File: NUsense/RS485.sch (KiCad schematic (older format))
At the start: 15 parts, among them J18? MOLEX22-03-5045, U21? MAX3443ECSA+

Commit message: Change hierarchy layout
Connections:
- net DXL_485+_1 renamed DXL_485+
- net DXL_485-_1 renamed DXL_485-
- net DXL_DIR_1 renamed DXL_DIR
- net DXL_RXD_1 renamed DXL_RXD
- net DXL_TXD_1 renamed DXL_TXD
- net VDD5o0V renamed +5V
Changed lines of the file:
@@
 LIBS:valves
 LIBS:ADM6713RAKS
+LIBS:Header_Connectors
 LIBS:MPU6000
 LIBS:NUbots
 LIBS:STM32F746ZGT6
-LIBS:Header_Connectors
 LIBS:NUsense-cache
 EELAYER 25 0
@@
 	1    0    0    -1
 $EndComp
-Text GLabel 3750 2550 1    60   Input ~ 0
-VDD5o0V
 $Comp
 L R R?
@@
 	1    0    0    -1
 $EndComp
-Text GLabel 6100 3500 2    60   Input ~ 0
-VDD5o0V
 $Comp
 L R R?
@@
 	0    -1   -1   0
 $EndComp
-Text GLabel 3550 3600 0    60   Input ~ 0
-DXL_DIR_1
-Text GLabel 3550 3500 0    60   Input ~ 0
-DXL_TXD_1
-Text GLabel 3550 3200 0    60   Input ~ 0
-DXL_RXD_1
-Text GLabel 7200 3200 2    60   Input ~ 0
-DXL_485+_1
-Text GLabel 7200 3300 2    60   Input ~ 0
-DXL_485-_1
-Text GLabel 3550 4850 0    60   Input ~ 0
-DXL_485+_1
-Text GLabel 3550 4950 0    60   Input ~ 0
-DXL_485-_1
 $Comp
 L GND #PWR?
@@
 	1    0    0    -1
 $EndComp
-Text GLabel 3850 4450 1    60   Input ~ 0
-DXL_PWR
 $Comp
 L C C?
@@
 	1    0    0    -1
 $EndComp
-Text GLabel 4950 9150 3    60   Input ~ 0
-DXL_PWR
 $Comp
 L R R?
@@
 	1    0    0    -1
 $EndComp
+$Comp
+L +5V #PWR?
+U 1 1 5A6FDCF8
+P 3750 2550
+F 0 "#PWR?" H 3750 2400 50  0001 C CNN
+F 1 "+5V" H 3750 2690 50  0000 C CNN
+F 2 "" H 3750 2550 50  0001 C CNN
+F 3 "" H 3750 2550 50  0001 C CNN
+	1    3750 2550
+	1    0    0    -1
+$EndComp
+Text HLabel 3550 3200 0    60   BiDi ~ 0
+DXL_RXD
+Text HLabel 3550 3500 0    60   BiDi ~ 0
+DXL_TXD
+Text HLabel 3550 3600 0    60   Input ~ 0
+DXL_DIR
+Text Label 3850 4450 1    60   ~ 0
+DXL_PWR
+Text Label 4950 9150 3    60   ~ 0
+DXL_PWR
+$Comp
+L +5V #PWR?
+U 1 1 5A6FED8C
+P 6100 3500
+F 0 "#PWR?" H 6100 3350 50  0001 C CNN
+F 1 "+5V" H 6100 3640 50  0000 C CNN
+F 2 "" H 6100 3500 50  0001 C CNN
+F 3 "" H 6100 3500 50  0001 C CNN
+	1    6100 3500
+	0    1    1    0
+$EndComp
+Text Label 7200 3200 0    60   ~ 0
+DXL_485+
+Text Label 7200 3300 0    60   ~ 0
+DXL_485-
+Text Label 3550 4850 2    60   ~ 0
+DXL_485+
+Text Label 3550 4950 2    60   ~ 0
+DXL_485-
 $EndSCHEMATC

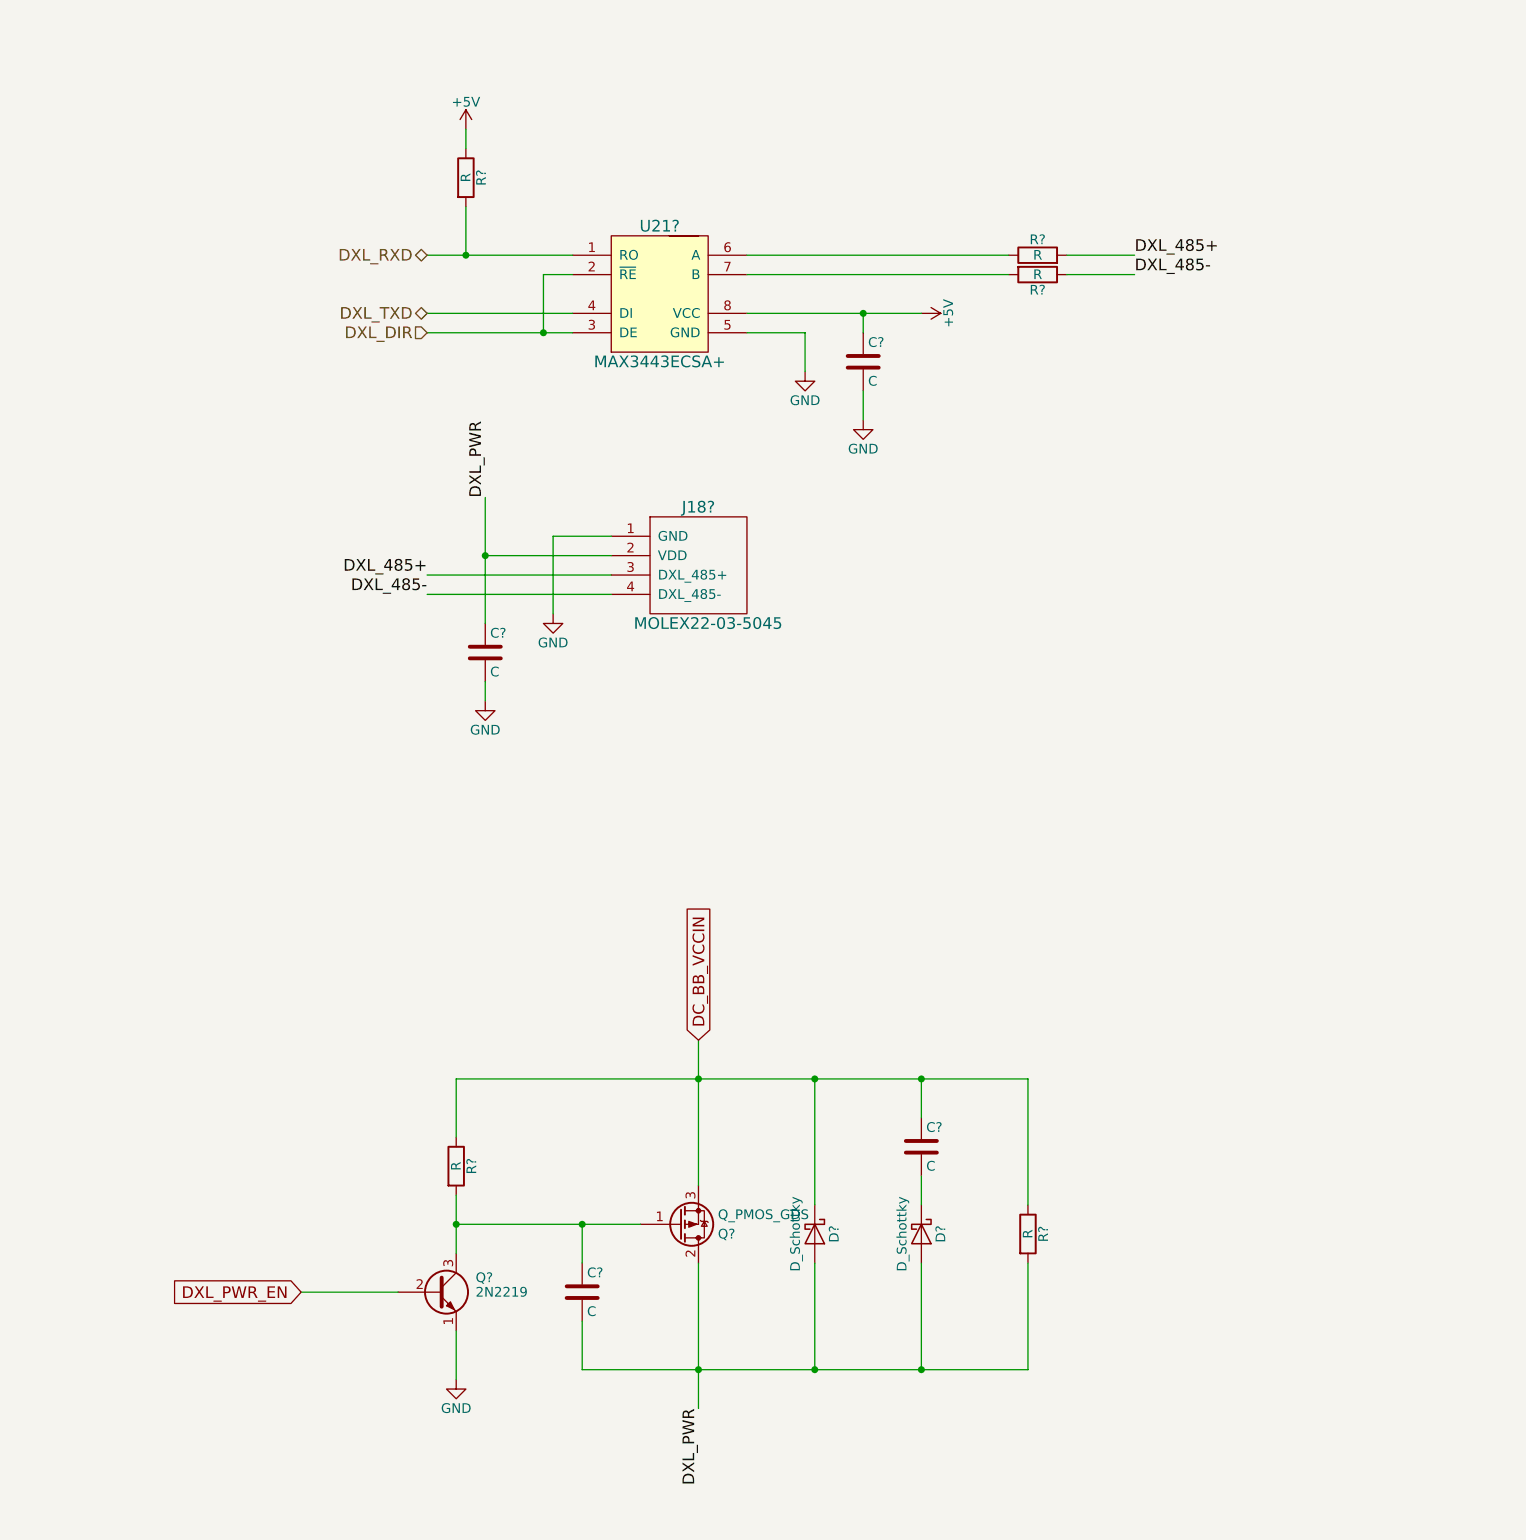
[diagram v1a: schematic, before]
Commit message: Update component values
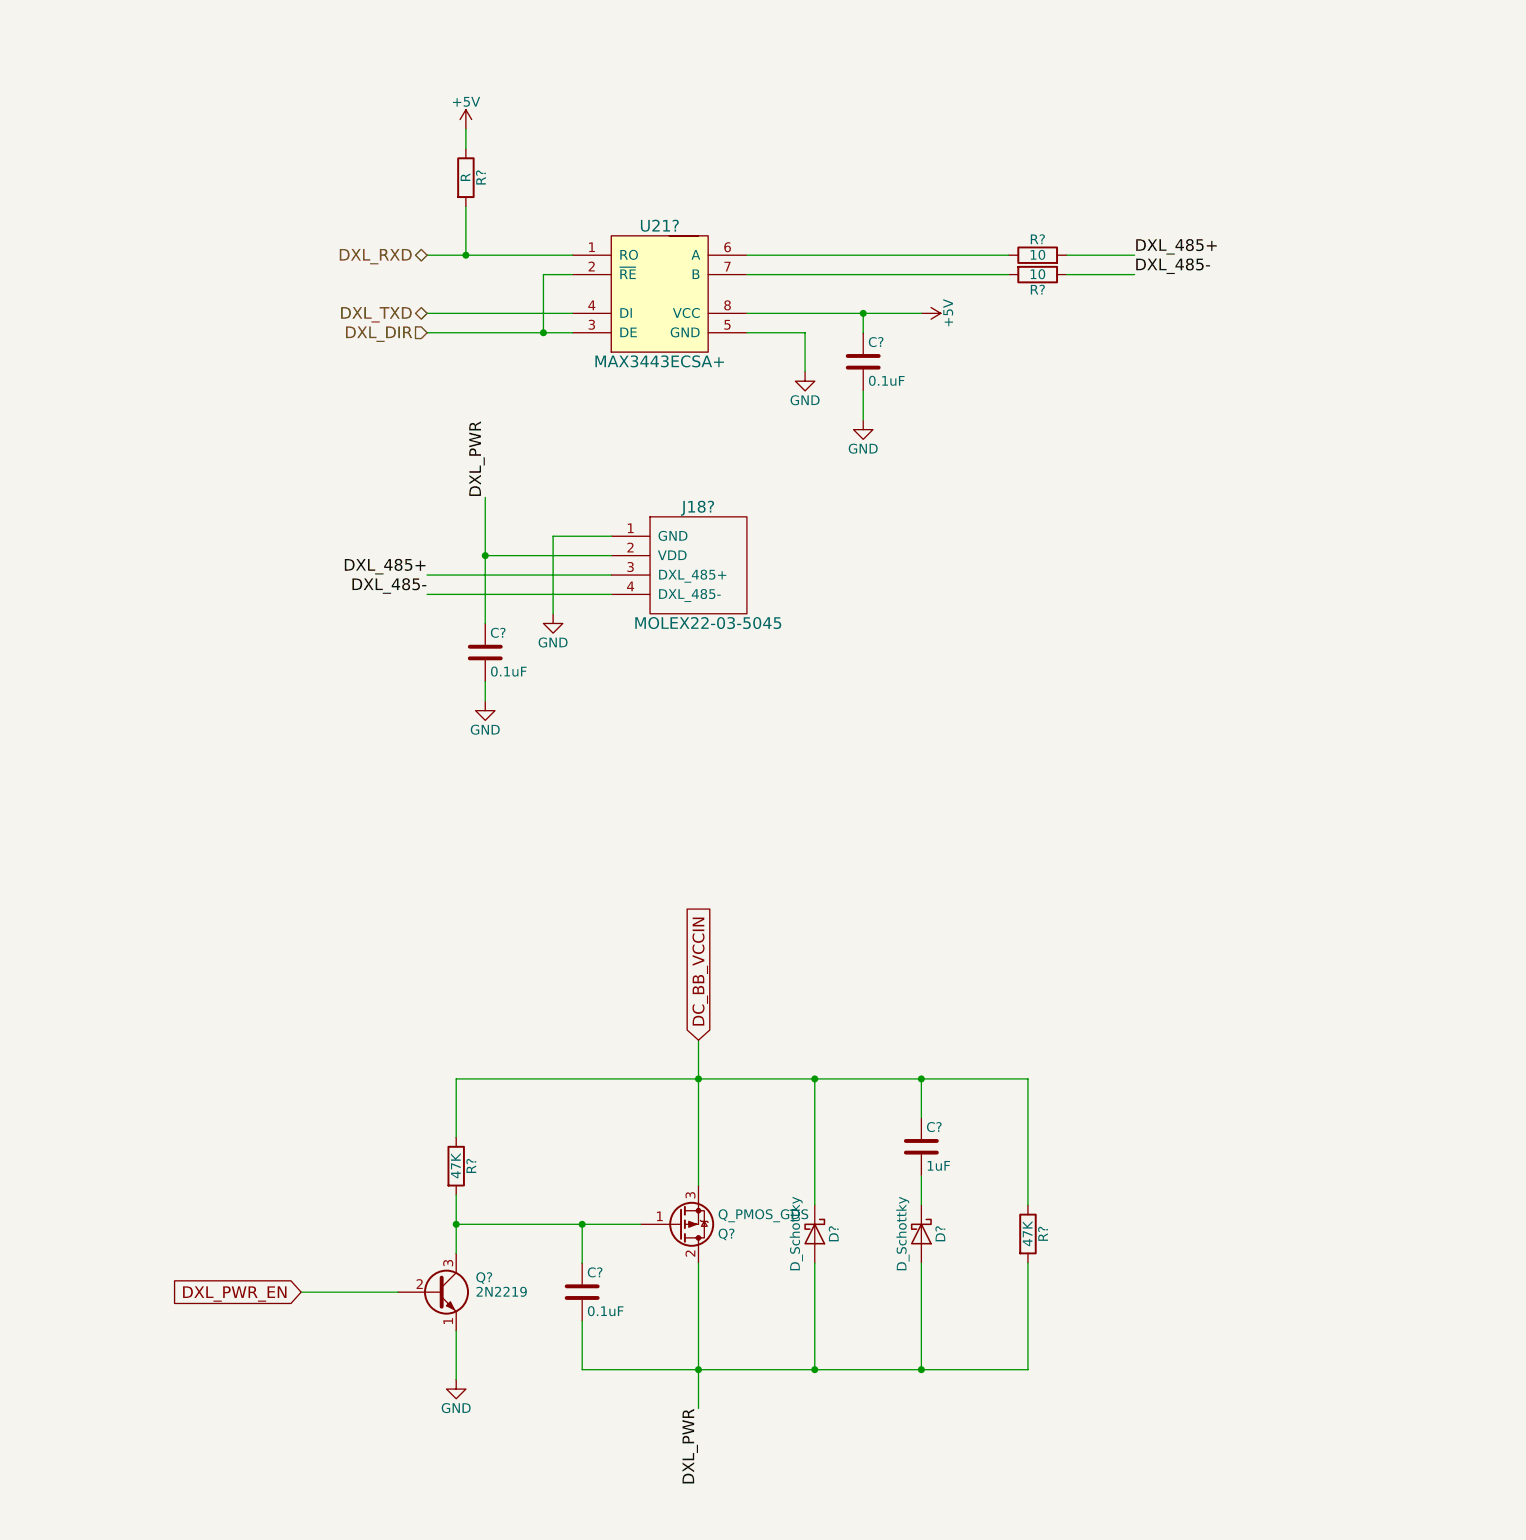
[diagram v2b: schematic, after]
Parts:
- C? (x3): value C -> 0.1uF
- C?: value C -> 1uF
- R? (x2): value R -> 10
- R? (x2): value R -> 47K
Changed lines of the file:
@@
 P 5800 3750
 F 0 "C?" H 5825 3850 50  0000 L CNN
-F 1 "C" H 5825 3650 50  0000 L CNN
+F 1 "0.1uF" H 5825 3650 50  0000 L CNN
 F 2 "" H 5838 3600 50  0001 C CNN
 F 3 "" H 5800 3750 50  0001 C CNN
@@
 P 6700 3300
 F 0 "R?" V 6780 3300 50  0000 C CNN
-F 1 "R" V 6700 3300 50  0000 C CNN
+F 1 "10" V 6700 3300 50  0000 C CNN
 F 2 "" V 6630 3300 50  0001 C CNN
 F 3 "" H 6700 3300 50  0001 C CNN
@@
 P 6700 3200
 F 0 "R?" V 6780 3200 50  0000 C CNN
-F 1 "R" V 6700 3200 50  0000 C CNN
+F 1 "10" V 6700 3200 50  0000 C CNN
 F 2 "" V 6630 3200 50  0001 C CNN
 F 3 "" H 6700 3200 50  0001 C CNN
@@
 P 3850 5250
 F 0 "C?" H 3875 5350 50  0000 L CNN
-F 1 "C" H 3875 5150 50  0000 L CNN
+F 1 "0.1uF" H 3875 5150 50  0000 L CNN
 F 2 "" H 3888 5100 50  0001 C CNN
 F 3 "" H 3850 5250 50  0001 C CNN
@@
 P 3700 7900
 F 0 "R?" V 3780 7900 50  0000 C CNN
-F 1 "R" V 3700 7900 50  0000 C CNN
+F 1 "47K" V 3700 7900 50  0000 C CNN
 F 2 "" V 3630 7900 50  0001 C CNN
 F 3 "" H 3700 7900 50  0001 C CNN
@@
 P 4350 8550
 F 0 "C?" H 4375 8650 50  0000 L CNN
-F 1 "C" H 4375 8450 50  0000 L CNN
+F 1 "0.1uF" H 4375 8450 50  0000 L CNN
 F 2 "" H 4388 8400 50  0001 C CNN
 F 3 "" H 4350 8550 50  0001 C CNN
@@
 P 6650 8250
 F 0 "R?" V 6730 8250 50  0000 C CNN
-F 1 "R" V 6650 8250 50  0000 C CNN
+F 1 "47K" V 6650 8250 50  0000 C CNN
 F 2 "" V 6580 8250 50  0001 C CNN
 F 3 "" H 6650 8250 50  0001 C CNN
@@
 P 6100 7800
 F 0 "C?" H 6125 7900 50  0000 L CNN
-F 1 "C" H 6125 7700 50  0000 L CNN
+F 1 "1uF" H 6125 7700 50  0000 L CNN
 F 2 "" H 6138 7650 50  0001 C CNN
 F 3 "" H 6100 7800 50  0001 C CNN

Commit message: Correct Broken Files
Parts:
- removed C?: 0.1uF, symbol C
- removed C?: 1uF, symbol C
- removed D? (x2): D_Schottky, symbol D_Schottky
- removed Q?: Q_PMOS_GDS, symbol Q_PMOS_GDS
- removed Q?: 2N2219, TO_SOT_Packages_THT:TO-39-3, symbol 2N2219
- removed R? (x2): 47K, symbol R
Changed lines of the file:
@@
-	1    0    0    -1
-$EndComp
-Text GLabel 2900 8550 0    60   Input ~ 0
-DXL_PWR_EN
-$Comp
-L R R?
-U 1 1 5A69947A
-P 3700 7900
-F 0 "R?" V 3780 7900 50  0000 C CNN
-F 1 "47K" V 3700 7900 50  0000 C CNN
-F 2 "" V 3630 7900 50  0001 C CNN
-F 3 "" H 3700 7900 50  0001 C CNN
-	1    3700 7900
-	1    0    0    -1
-$EndComp
-$Comp
-L C C?
-U 1 1 5A69952D
-P 4350 8550
-F 0 "C?" H 4375 8650 50  0000 L CNN
-F 1 "0.1uF" H 4375 8450 50  0000 L CNN
-F 2 "" H 4388 8400 50  0001 C CNN
-F 3 "" H 4350 8550 50  0001 C CNN
-	1    4350 8550
-	1    0    0    -1
-$EndComp
-$Comp
-L R R?
-U 1 1 5A699733
-P 6650 8250
-F 0 "R?" V 6730 8250 50  0000 C CNN
-F 1 "47K" V 6650 8250 50  0000 C CNN
-F 2 "" V 6580 8250 50  0001 C CNN
-F 3 "" H 6650 8250 50  0001 C CNN
-	1    6650 8250
-	1    0    0    -1
-$EndComp
-Text GLabel 4950 7250 1    60   Input ~ 0
-DC_BB_VCCIN
-$Comp
-L D_Schottky D?
-U 1 1 5A699A5F
-P 5550 8250
-F 0 "D?" H 5550 8350 50  0000 C CNN
-F 1 "D_Schottky" H 5550 8150 50  0000 C CNN
-F 2 "" H 5550 8250 50  0001 C CNN
-F 3 "" H 5550 8250 50  0001 C CNN
-	1    5550 8250
-	0    1    1    0
-$EndComp
-$Comp
-L D_Schottky D?
-U 1 1 5A699B12
-P 6100 8250
-F 0 "D?" H 6100 8350 50  0000 C CNN
-F 1 "D_Schottky" H 6100 8150 50  0000 C CNN
-F 2 "" H 6100 8250 50  0001 C CNN
-F 3 "" H 6100 8250 50  0001 C CNN
-	1    6100 8250
-	0    1    1    0
-$EndComp
-$Comp
-L C C?
-U 1 1 5A699B46
-P 6100 7800
-F 0 "C?" H 6125 7900 50  0000 L CNN
-F 1 "1uF" H 6125 7700 50  0000 L CNN
-F 2 "" H 6138 7650 50  0001 C CNN
-F 3 "" H 6100 7800 50  0001 C CNN
-	1    6100 7800
-	1    0    0    -1
-$EndComp
-$Comp
-L Q_PMOS_GDS Q?
-U 1 1 5A699B87
-P 4850 8200
-F 0 "Q?" H 5050 8250 50  0000 L CNN
-F 1 "Q_PMOS_GDS" H 5050 8150 50  0000 L CNN
-F 2 "" H 5050 8300 50  0001 C CNN
-F 3 "" H 4850 8200 50  0001 C CNN
-	1    4850 8200
-	1    0    0    1
-$EndComp
-$Comp
-L 2N2219 Q?
-U 1 1 5A69A90B
-P 3600 8550
-F 0 "Q?" H 3800 8625 50  0000 L CNN
-F 1 "2N2219" H 3800 8550 50  0000 L CNN
-F 2 "TO_SOT_Packages_THT:TO-39-3" H 3800 8475 50  0001 L CIN
-F 3 "" H 3600 8550 50  0001 L CNN
-	1    3600 8550
 	1    0    0    -1
 $EndComp
@@
 Wire Wire Line
 	4200 4650 4500 4650
-Wire Wire Line
-	4950 8400 4950 9150
-Wire Wire Line
-	4350 8950 6650 8950
-Wire Wire Line
-	4350 8950 4350 8700
-Wire Wire Line
-	6650 8950 6650 8400
-Connection ~ 4950 8950
-Wire Wire Line
-	3700 7750 3700 7450
-Wire Wire Line
-	3700 7450 6650 7450
-Wire Wire Line
-	6650 7450 6650 8100
-Wire Wire Line
-	4950 7250 4950 8000
-Connection ~ 4950 7450
-Wire Wire Line
-	4650 8200 3700 8200
-Wire Wire Line
-	4350 8400 4350 8200
-Connection ~ 4350 8200
-Wire Wire Line
-	5550 8100 5550 7450
-Connection ~ 5550 7450
-Wire Wire Line
-	6100 7650 6100 7450
-Connection ~ 6100 7450
-Wire Wire Line
-	6100 7950 6100 8100
-Wire Wire Line
-	6100 8400 6100 8950
-Connection ~ 6100 8950
-Wire Wire Line
-	5550 8400 5550 8950
-Connection ~ 5550 8950
-Wire Wire Line
-	3700 8050 3700 8350
-Connection ~ 3700 8200
-$Comp
-L GND #PWR?
-U 1 1 5A69AA92
-P 3700 9000
-F 0 "#PWR?" H 3700 8750 50  0001 C CNN
-F 1 "GND" H 3700 8850 50  0000 C CNN
-F 2 "" H 3700 9000 50  0001 C CNN
-F 3 "" H 3700 9000 50  0001 C CNN
-	1    3700 9000
-	1    0    0    -1
-$EndComp
-Wire Wire Line
-	3700 9000 3700 8750
-Wire Wire Line
-	3400 8550 2900 8550
 $Comp
 L MOLEX22-03-5045 J18?
@@
 Text HLabel 3550 3600 0    60   Input ~ 0
 DXL_DIR
-Text Label 3850 4450 1    60   ~ 0
-DXL_PWR
-Text Label 4950 9150 3    60   ~ 0
-DXL_PWR
 $Comp
 L +5V #PWR?
@@
 Text Label 3550 4950 2    60   ~ 0
 DXL_485-
+Text HLabel 3850 4450 0    60   Input ~ 0
+DXL_PWR
 $EndSCHEMATC

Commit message: ESD protection
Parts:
- added U?: AVRC5S_05D_050_050R, symbol AVRC5S_05D_050_050R
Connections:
- net DXL_RXD: now also U?.3 (B1); no longer R?.2, U21?.1 (RO)
- net DXL_TXD: now also U?.2 (A1); no longer U21?.4 (DI)
- net GND: now also U?.1 (GND)
- new net: R?.2, U21?.1 (RO), U?.6 (B2)
- new net: U21?.4 (DI), U?.5 (A2)
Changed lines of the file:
@@
 $EndComp
 Wire Wire Line
-	3550 3600 4300 3600
+	3550 3600 4150 3600
+Wire Wire Line
+	4150 3600 4300 3600
 Wire Wire Line
 	4300 3500 3550 3500
 Wire Wire Line
-	3550 3200 4300 3200
+	3550 3200 3750 3200
+Wire Wire Line
+	3750 3200 4300 3200
 Wire Wire Line
 	4300 3300 4150 3300
@@
 	5200 3300 6550 3300
 Wire Wire Line
-	5200 3500 6100 3500
+	5200 3500 5800 3500
+Wire Wire Line
+	5800 3500 6100 3500
 Wire Wire Line
 	5800 3600 5800 3500
@@
 	3850 5500 3850 5400
 Wire Wire Line
-	3850 4450 3850 5100
+	3850 4450 3850 4750
+Wire Wire Line
+	3850 4750 3850 5100
 Wire Wire Line
 	3850 4750 4500 4750
@@
 	1    0    0    -1
 $EndComp
-Text HLabel 3550 3200 0    60   BiDi ~ 0
+Text HLabel 1950 3300 0    60   BiDi ~ 0
 DXL_RXD
-Text HLabel 3550 3500 0    60   BiDi ~ 0
+Text HLabel 1950 3400 0    60   BiDi ~ 0
 DXL_TXD
 Text HLabel 3550 3600 0    60   Input ~ 0
@@
 Text HLabel 3850 4450 0    60   Input ~ 0
 DXL_PWR
+$Comp
+L AVRC5S_05D_050_050R U?
+U 1 1 5A72D5C4
+P 2150 3600
+F 0 "U?" H 2400 4050 60  0000 C CNN
+F 1 "AVRC5S_05D_050_050R" H 2450 3550 60  0000 C CNN
+F 2 "" H 2150 3600 60  0001 C CNN
+F 3 "" H 2150 3600 60  0001 C CNN
+	1    2150 3600
+	1    0    0    -1
+$EndComp
+Wire Wire Line
+	2850 3300 3550 3300
+Wire Wire Line
+	3550 3300 3550 3200
+Wire Wire Line
+	3550 3500 3550 3400
+Wire Wire Line
+	3550 3400 2850 3400
+Wire Wire Line
+	1950 3500 1850 3500
+Wire Wire Line
+	1850 3500 1850 3800
+$Comp
+L GND #PWR?
+U 1 1 5A72D76F
+P 1850 3800
+F 0 "#PWR?" H 1850 3550 50  0001 C CNN
+F 1 "GND" H 1850 3650 50  0000 C CNN
+F 2 "" H 1850 3800 50  0001 C CNN
+F 3 "" H 1850 3800 50  0001 C CNN
+	1    1850 3800
+	1    0    0    -1
+$EndComp
 $EndSCHEMATC
